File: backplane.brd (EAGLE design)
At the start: 153.7 x 128.3 mm, 45 parts, among them J1 L717HDE15PD4CH4R, J10 5013310807, J11 5013310807, J12 5013310807, J13 5013310807, J14 5013311007, J15 5013311007, J16 5013311007, J17 5013311007, J18 5013311007, J19 5013311007, J2 1054301102, J20 5013311007, J21 5013311007, J22 5013311007, J23 5013311007, J24 SEAM-40-03.0-S-06-2-A-K-TR, J25 5055670271, J3 5011902017, J4 5013310807, J5 5013310807, J6 5013310807, J7 5013310807, J8 5013310807, J9 5013310807, U1 AM26LV32EIPWR, U10 AM26LV32EIPWR, U2 AM26LV32EIPWR, U3 AM26LV32EIPWR, U4 AM26LV32EIPWR, U5 AM26LV32EIPWR, U6 AM26LV32EIPWR, U7 AM26LV32EIPWR, U8 AM26LV32EIPWR, U9 AM26LV32EIPWR

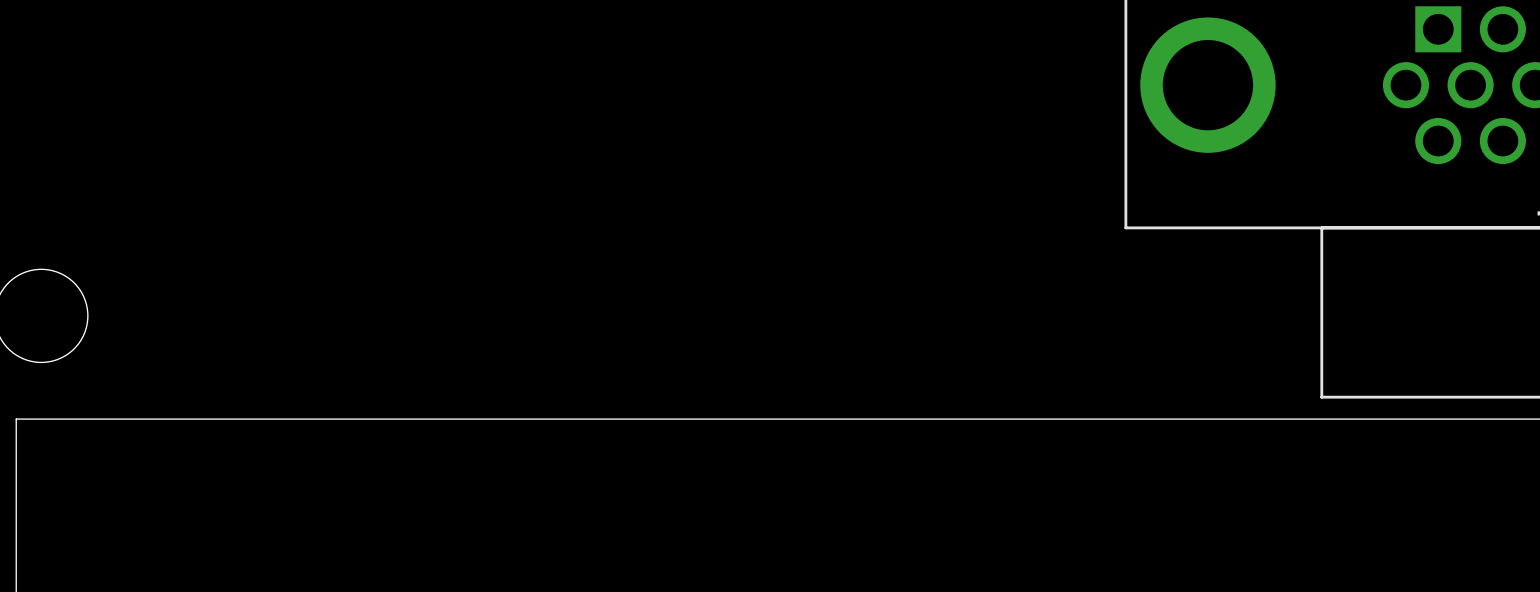
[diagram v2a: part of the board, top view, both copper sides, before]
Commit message: adjusted silkscreen
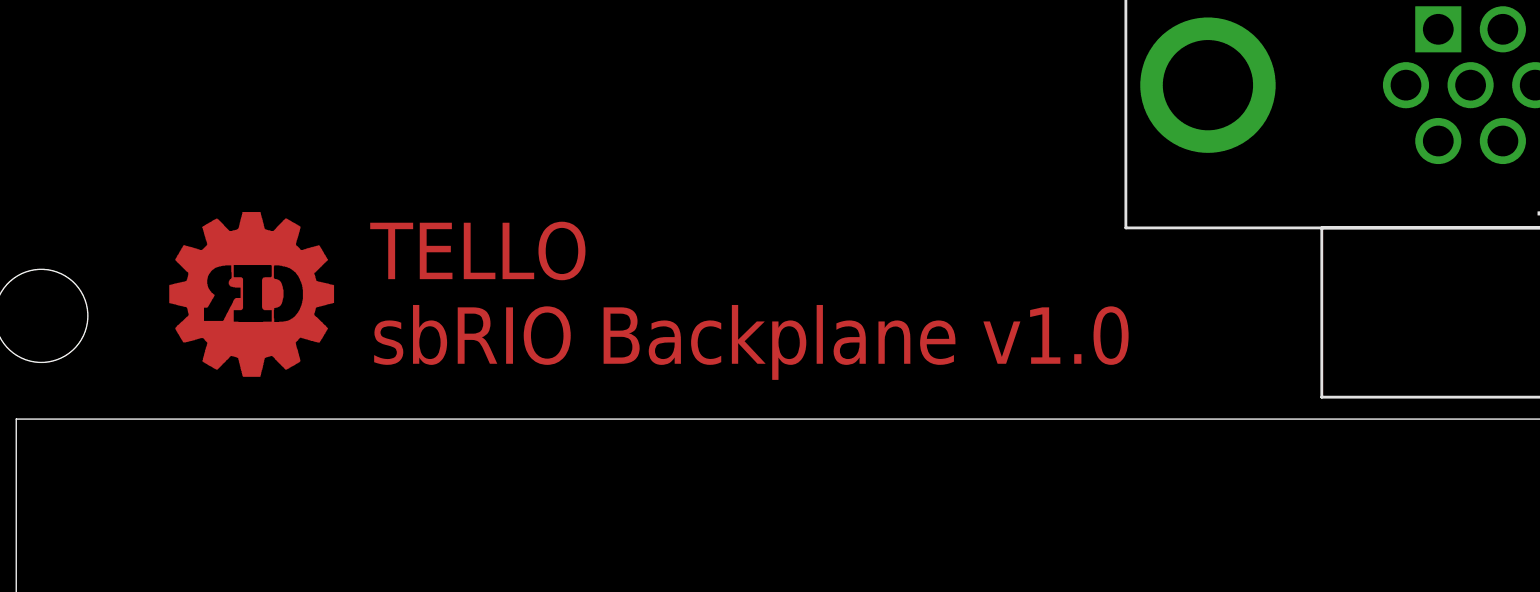
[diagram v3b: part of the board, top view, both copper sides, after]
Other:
- board text added: "TELLO sbRIO Backplane v1.0"

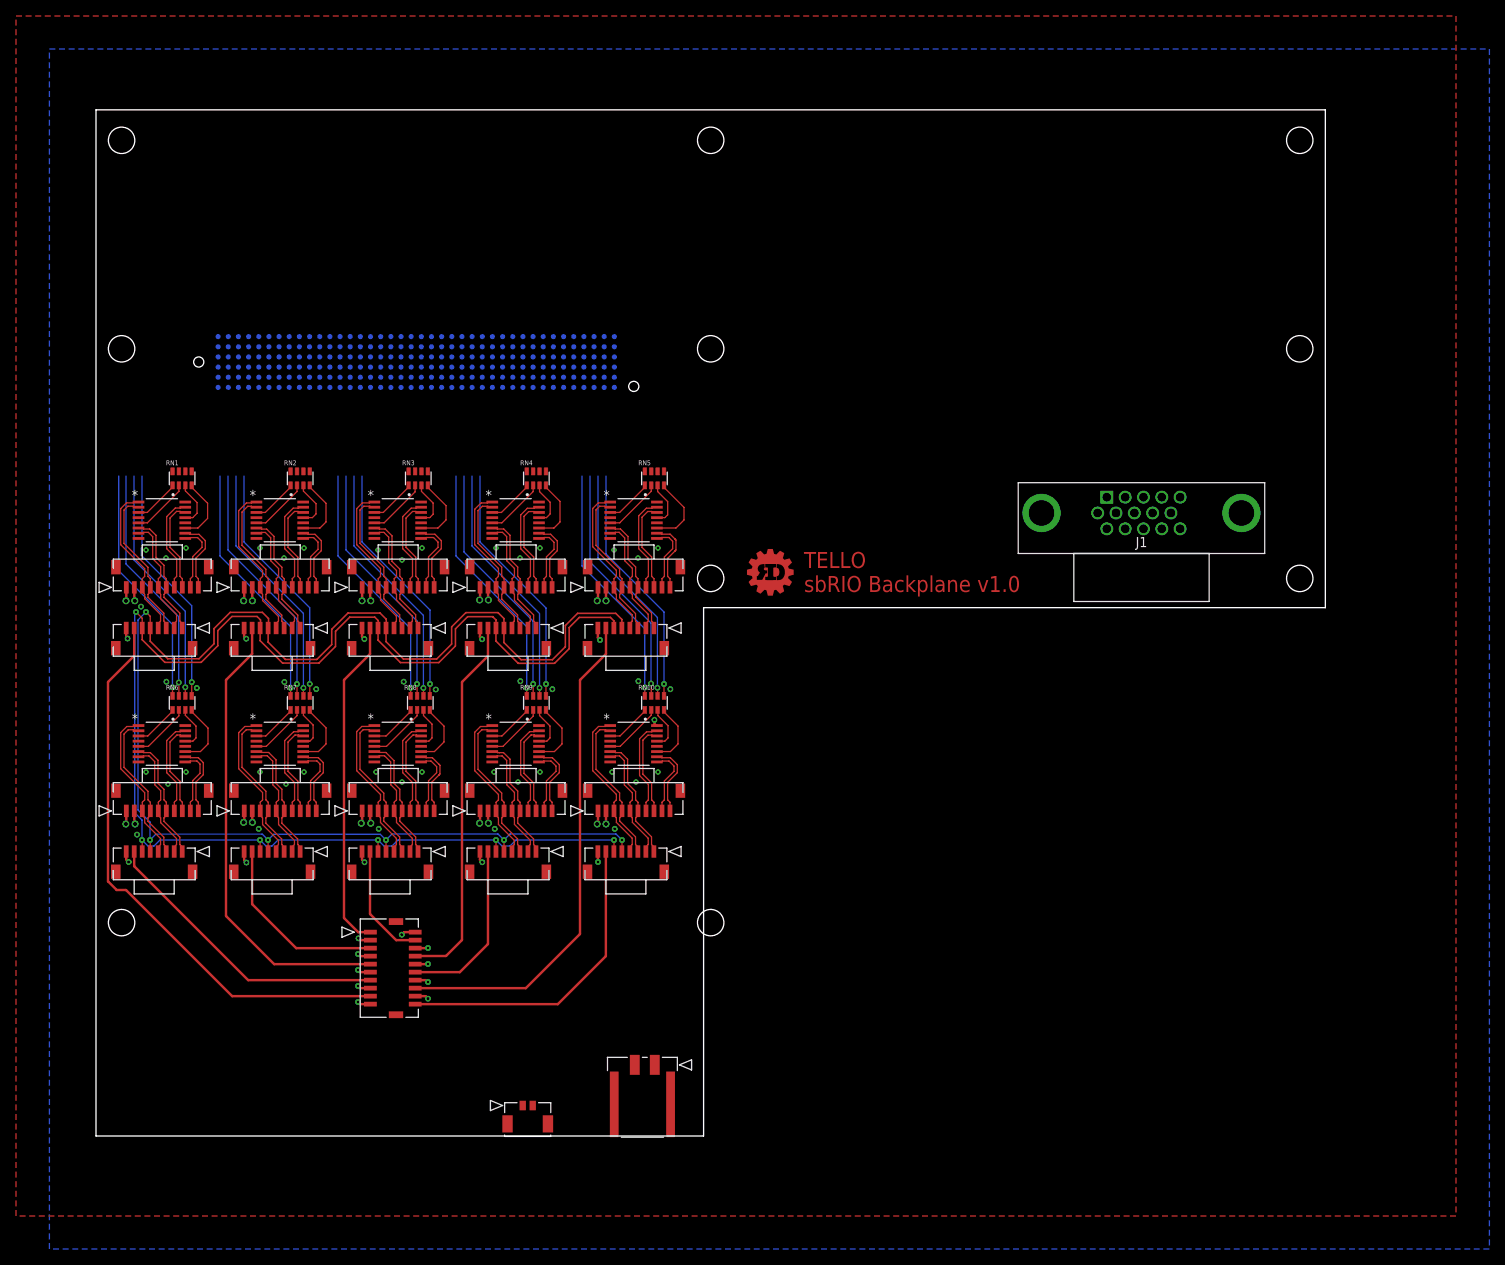
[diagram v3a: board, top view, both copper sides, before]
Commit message: many RMC connections routed
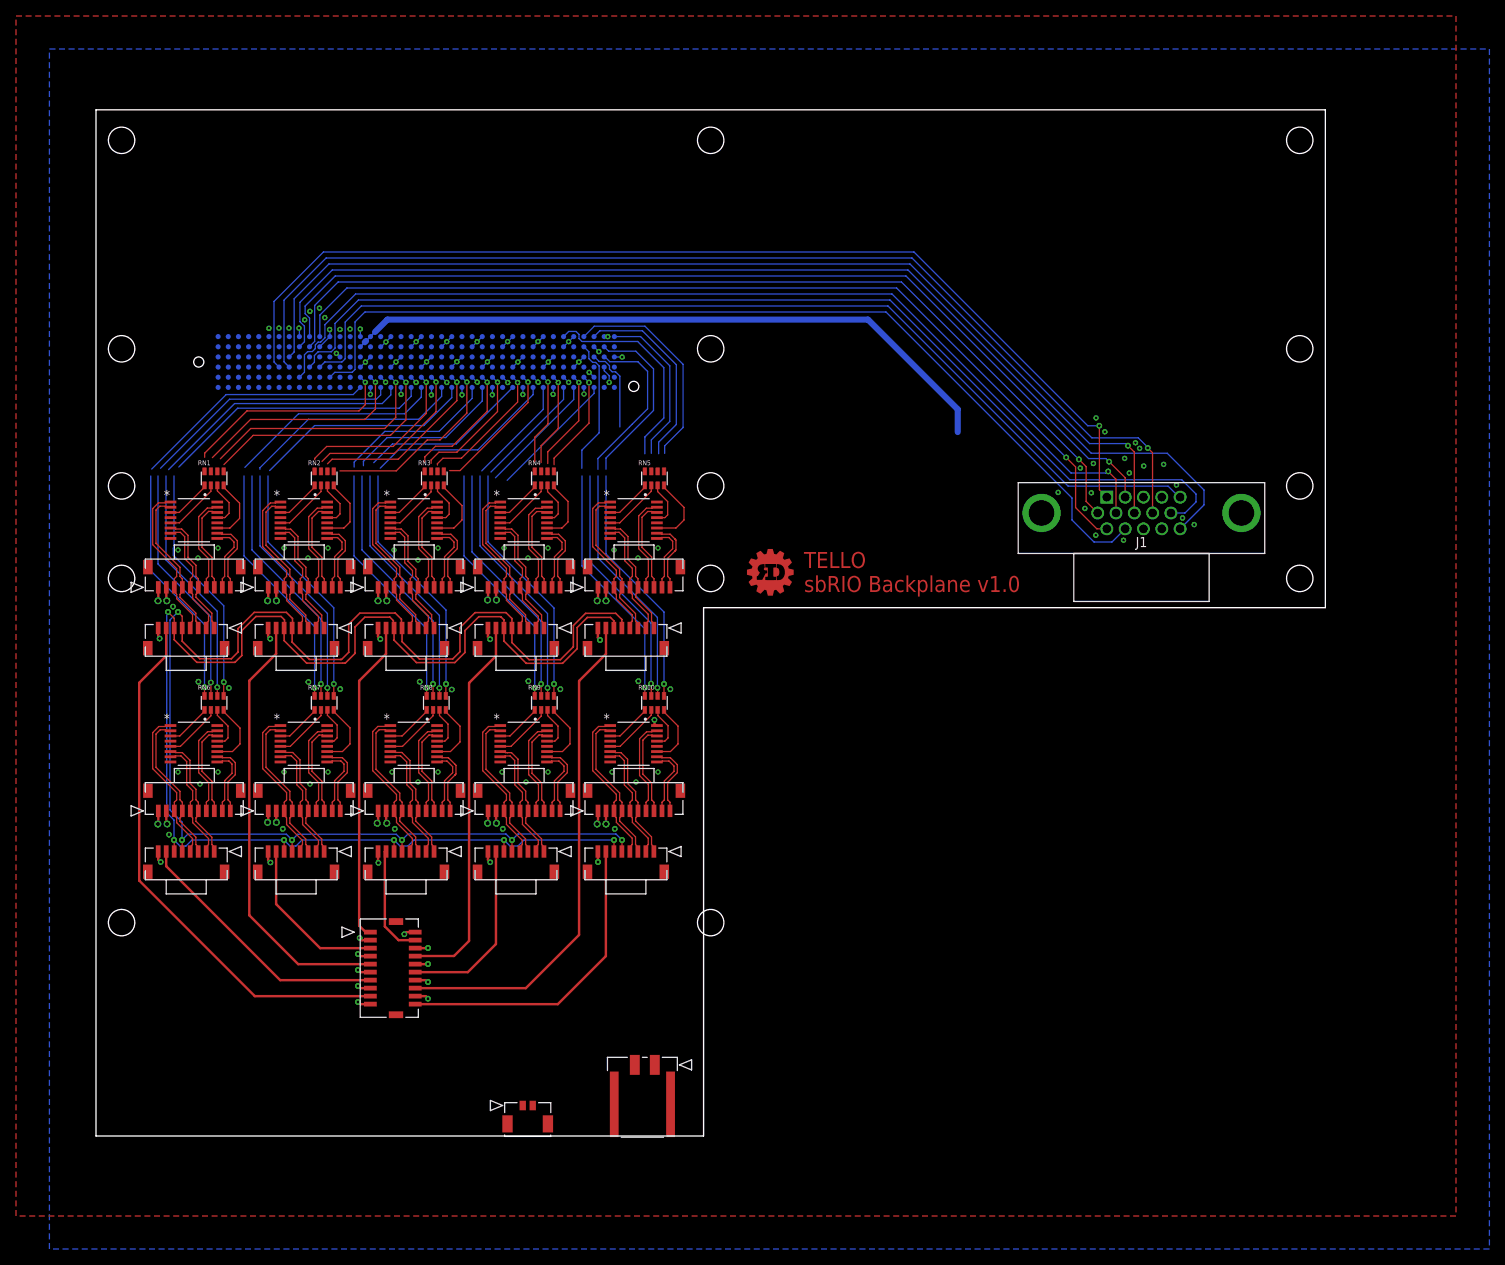
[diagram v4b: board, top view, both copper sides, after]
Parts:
- moved J14 4.00 mm to (7.79, 68.6)
- moved J19 4.00 mm to (7.79, 40.6)
- moved J4 4.00 mm to (14.8, 63.5)
- moved J9 4.00 mm to (14.8, 35.6)
- moved RN1 4.00 mm to (14.8, 82.2)
- moved RN6 4.00 mm to (14.8, 54.1)
- moved U1 4.00 mm to (12.2, 77.0)
- moved U6 4.00 mm to (12.2, 49.0)
- moved J10 3.00 mm to (28.5, 35.6)
- moved J15 3.00 mm to (21.5, 68.6)
- moved J20 3.00 mm to (21.5, 40.6)
- moved J5 3.00 mm to (28.5, 63.5)
- moved RN2 3.00 mm to (28.5, 82.2)
- moved RN7 3.00 mm to (28.5, 54.1)
- moved U2 3.00 mm to (26.0, 77.0)
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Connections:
- new net 5V_C_SERIES: J24.A16, J24.B15
- new net 5V_FILT: J1.4
- new net CVRT#_DIO3[1]: J1.9, J24.D8
- new net DIO0: J24.F38
- new net DIO1: J24.F36
- new net DIO10: J24.F23
- new net DIO11: J24.F21
- new net DIO12: J24.F20
- new net DIO13: J24.F18
- new net DIO14: J24.F17
- new net DIO15: J24.F15
- new net DIO16: J24.C39
- new net DIO17: J24.C38
- new net DIO2: J24.F35
- new net DIO3: J24.F33
- new net DIO32: J24.E37
- new net DIO33: J24.E36
- new net DIO34: J24.E34
- new net DIO35: J24.E33
- new net DIO36: J24.E31
- new net DIO37: J24.E30
- new net DIO38: J24.E28
- new net DIO39: J24.E27
- new net DIO4: J24.F32
- new net DIO40: J24.E25
- new net DIO41: J24.E24
- new net DIO42: J24.E22
- new net DIO43: J24.E21
- new net DIO44: J24.E19
- new net DIO45: J24.E18
- new net DIO46: J24.E16
- new net DIO47: J24.E15
- new net DIO48: J24.B39
- new net DIO49: J24.B37
- new net DIO5: J24.F30
- new net DIO6: J24.F29
- new net DIO64: J24.D38
- new net DIO65: J24.D37
- new net DIO66: J24.D35
- new net DIO67: J24.D34
- new net DIO68: J24.D32
- new net DIO69: J24.D31
- new net DIO7: J24.F27
- new net DIO70: J24.D29
- new net DIO71: J24.D28
- new net DIO72: J24.D26
- new net DIO73: J24.D25
- new net DIO74: J24.D23
- new net DIO75: J24.D22
- new net DIO76: J24.D20
- new net DIO77: J24.D19
- new net DIO78: J24.D17
- new net DIO79: J24.D16
- new net DIO8: J24.F26
- new net DIO80: J24.A40
- new net DIO81: J24.A38
- new net DIO82: J24.A37
- new net DIO83: J24.A35
- new net DIO84: J24.A34
- new net DIO9: J24.F24
- new net DONE#_DIO2[1]: J1.15, J24.B9
- new net ID_SELECT#[1]: J1.1, J24.D7
- new net MISO_DIO6[1]: J1.12, J24.E12
- new net MOSI_DIO7[1]: J1.6, J24.B10
- new net OSCLK_DIO0[1]: J1.10, J24.D10
- new net SLEEP[1]: J1.8, J24.C8
- new net SPICS#_DIO5[1]: J1.2, J24.A10
- new net SPIFUNC_DIO4[1]: J1.7, J24.E9
- new net SPI_CLK[1]: J1.11, J24.A11
- new net TRIG_DIO1[1]: J1.5, J24.D11
- net GND: now also J1.14, J1.MH1, J1.MH2, J24.A12, J24.A15, J24.A18, J24.A21, J24.A24, J24.A27, J24.A3, J24.A30, J24.A33, J24.A36, J24.A39, J24.A4, J24.A9, J24.B1, J24.B11, J24.B14, J24.B17, J24.B2, J24.B20, J24.B23, J24.B26, J24.B29, J24.B32, J24.B35, J24.B38, J24.B5, J24.B8, J24.C10, J24.C13, J24.C16, J24.C19, J24.C22, J24.C25, J24.C28, J24.C3, J24.C31, J24.C34, J24.C37, J24.C4, J24.C40, J24.C7, J24.D1, J24.D12, J24.D15, J24.D18, J24.D2, J24.D21, J24.D24, J24.D27, J24.D30, J24.D33, J24.D36, J24.D39, J24.D5, J24.D9, J24.E11, J24.E14, J24.E17, J24.E20, J24.E23, J24.E26, J24.E29, J24.E3, J24.E32, J24.E35, J24.E38, J24.E4, J24.E7, J24.E8, J24.F1, J24.F13, J24.F16, J24.F19, J24.F2, J24.F22, J24.F25, J24.F28, J24.F31, J24.F34, J24.F37, J24.F5, J24.F6
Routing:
- net DONE#_DIO2[1]: track 0.00 -> 138.2 mm
- net CVRT#_DIO3[1]: track 0.00 -> 137.1 mm, vias 0 -> 1
- net ID_SELECT#[1]: track 0.00 -> 132.5 mm, vias 0 -> 1
- net SLEEP[1]: track 0.00 -> 131.7 mm, vias 0 -> 1
- net OSCLK_DIO0[1]: track 0.00 -> 131.3 mm
- net TRIG_DIO1[1]: track 0.00 -> 123.5 mm
- net SPIFUNC_DIO4[1]: track 0.00 -> 122.9 mm, vias 0 -> 1
- net SPICS#_DIO5[1]: track 0.00 -> 121.0 mm, vias 0 -> 1
- net MISO_DIO6[1]: track 0.00 -> 120.5 mm
- net MOSI_DIO7[1]: track 0.00 -> 119.0 mm, vias 0 -> 1
- net SPI_CLK[1]: track 0.00 -> 117.9 mm, vias 0 -> 1
- net 5V_C_SERIES: track 0.00 -> 83.8 mm
- net GND: track 16.4 -> 67.6 mm, vias 56 -> 122
- net DIO12: track 0.00 -> 33.8 mm
- net DIO13: track 0.00 -> 32.6 mm
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- added copper zone on layer 15, net 5V_SBRIO
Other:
- board text added: "DO MOUNTING HOLES NEED TO BE GROUNDED"
